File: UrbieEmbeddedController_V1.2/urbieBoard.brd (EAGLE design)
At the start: 100 x 80 mm, 84 parts, among them IC1 IC_FT311D-LQFP-32, J1 DURACLIK-4SMD, Q1 PFET, Q2 2N3904, U2 MAX232TSSOP, Y3 12mHz

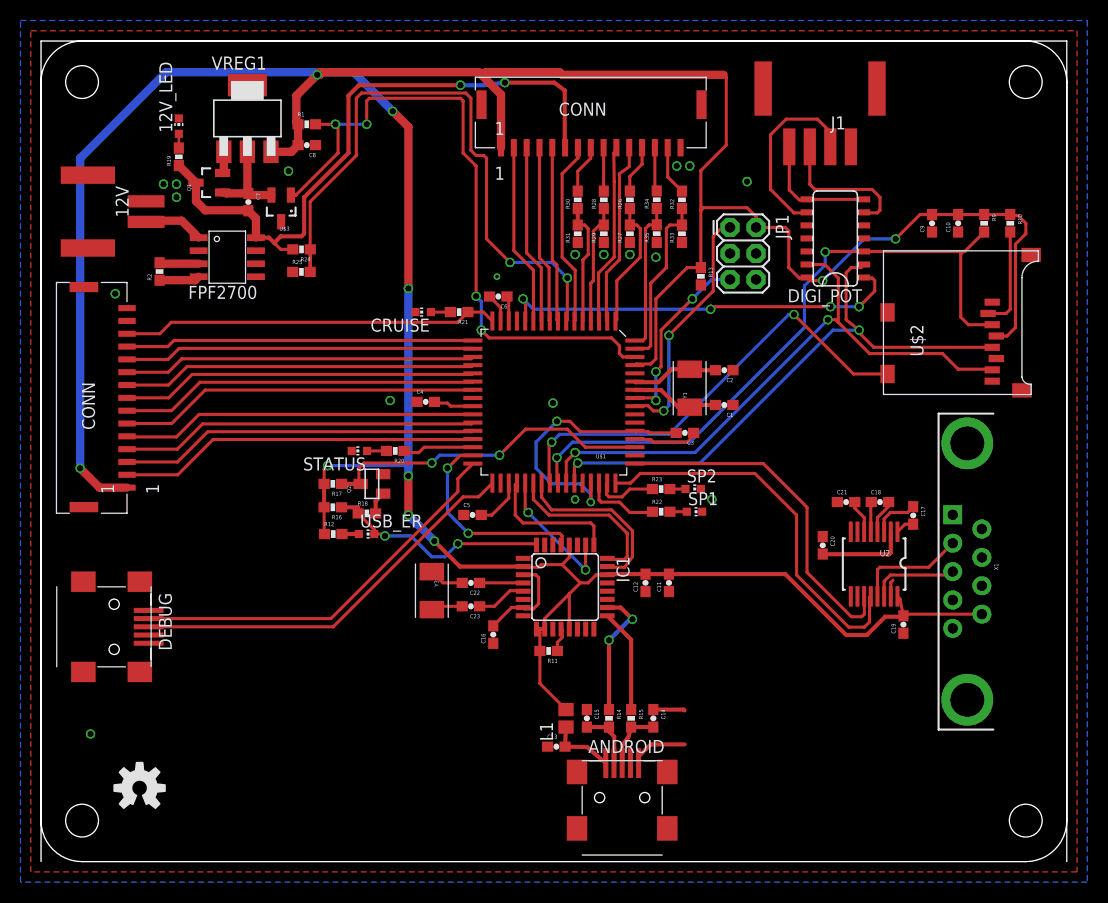
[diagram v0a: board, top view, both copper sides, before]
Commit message: Additions to Version 1.2
Added the 12V to 5V regulator circuit
Fixed SPI SS lines
Added SPI Header
Added TWI Header
Added Silkscreen
TODO: Adjust voltage divider values to get max 2.5V for ADCs
TODO: Pull TWI lines to high
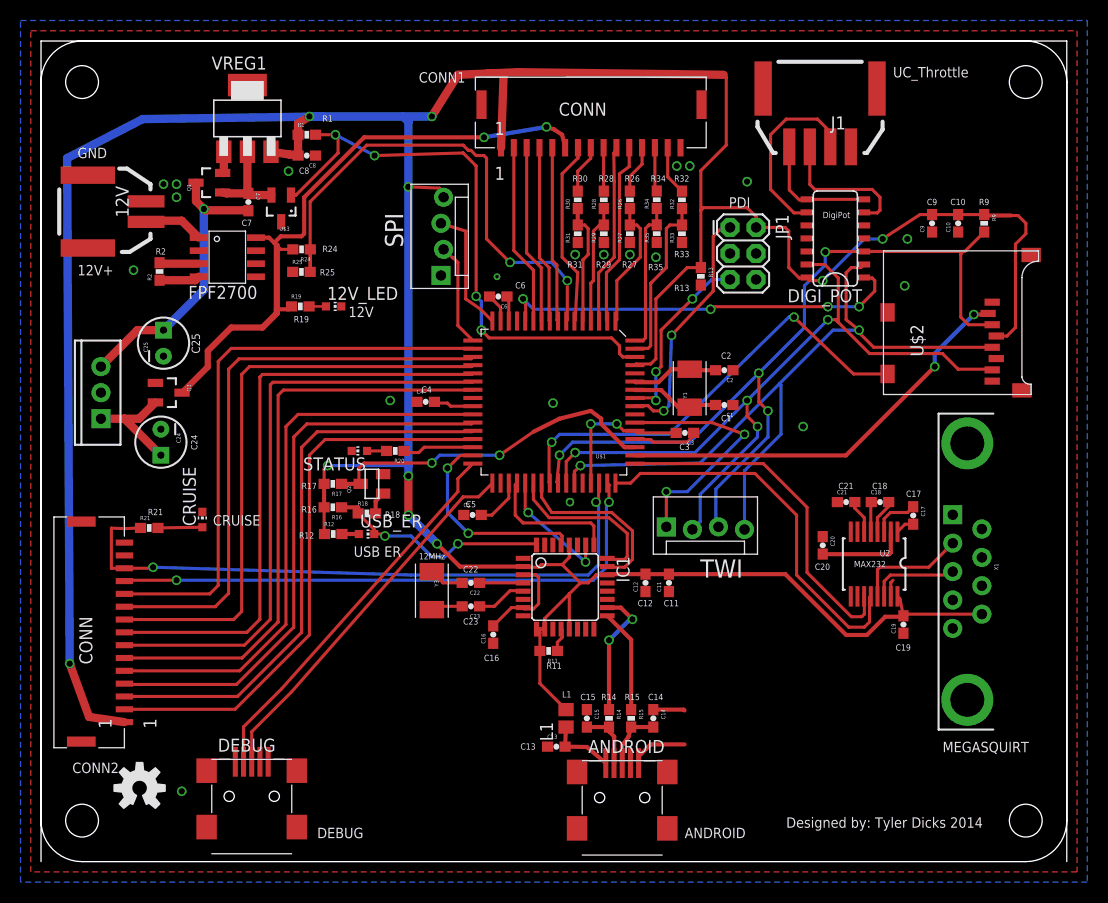
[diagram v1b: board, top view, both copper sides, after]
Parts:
- removed R10: 100K, SparkFun-Passives:0603-RES
- removed R22, R23: 620, SparkFun-Passives:0603-RES
- removed SP1, SP2: (no value), adafruit:CHIP-LED0603
- added C24, C25: (no value), SparkFun-Passives:CPOL-RADIAL-10UF-25V
- added IC2: (no value), SparkFun-PowerIC:TO220-IGO
- added JP3: (no value), SparkFun-Connectors:MOLEX-1X4_LOCK
- added Q3: MOSFET-PCHANNELSMD, SparkFun-DiscreteSemi:SOT23-3
- added SPI: SPI, SparkFun-Connectors:MOLEX-1X4_LOCK
- moved R21 36.8 mm to (10.5, 32.5), turned to 0 degrees
- moved U$6 30.5 mm to (67.6, 7.37)
- moved CRUISE 29.5 mm to (15.7, 33.4), turned to 0 degrees
- moved 12V_LED 23.2 mm to (28.5, 54.1), turned to 270 degrees
- moved U$9 22.9 mm to (8.13, 22.4)
- moved DEBUG 22.7 mm to (20.5, 5.37), turned to 0 degrees
- moved U$5 22.5 mm to (27.7, 7.62)
- moved U$4 21.9 mm to (28.2, 13.0)
- moved R19 18.8 mm to (25.3, 54.1), turned to 0 degrees
- moved R1 1.02 mm to (25.9, 70.9)
- moved C8 1.02 mm to (25.9, 68.8)
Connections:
- removed net CRUISE_ENABLE: U$9.14
- removed net N$17: R10.2, U$2.2
- removed net N$32: R22.2, SP1.A
- removed net N$34: R23.2, SP2.A
- removed net SPARE: U$1.50
- removed net SPARE_LED1: R22.1, U$1.46
- removed net SPARE_LED2: R23.1, U$1.47
- new net 5V_REG: C25.1, C7.2, IC2.OUT, Q1.3
- new net I2C_SCL: JP3.2, U$1.17
- new net I2C_SDA: JP3.3, U$1.16
- new net N$14: C24.1, IC2.IN, Q3.2
- new net SD_CS: U$1.50, U$2.2
- net 3.3V: now also JP3.4; no longer R10.1
- net CRUISE_ON: now also U$1.46; no longer U$1.16
- net DRIVE_ENABLE: now also U$1.47; no longer U$1.17
- net GND: now also C24.2, C25.2, IC2.GND, JP3.1, Q3.1; no longer SP1.C, SP2.C
- net SD_MISO: now also SPI.2
- net SD_MOSI: now also SPI.3
- net SD_SCK: now also SPI.4
- net SPARE2: now also SPI.1
- net V_BATT: now also Q3.3; no longer C7.2, Q1.3
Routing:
- net SD_CS: track 0.00 -> 40.9 mm, vias 0 -> 2
- net 5V_REG: track 0.00 -> 28.3 mm, vias 0 -> 1
- net CRUISE_ON: track 36.9 -> 62.9 mm, vias 0 -> 2
- net SPARE2: track 0.00 -> 24.2 mm, vias 0 -> 2
- net CAP_ON: track 34.7 -> 58.3 mm
- net GEN_STOP: track 34.5 -> 57.8 mm
- net MC_ON: track 34.9 -> 58.0 mm
- net MC_ENABLE: track 35.1 -> 57.7 mm
- net GEN_START: track 34.3 -> 56.9 mm
- net DRIVE_DISABLE: track 34.2 -> 56.7 mm
- net DRIVE_ENABLE: track 34.0 -> 56.1 mm, vias 0 -> 2
- net EFI_IN: track 34.7 -> 55.6 mm
- net STARTING_IN: track 34.8 -> 55.4 mm
- net MC_ON_IN: track 35.0 -> 55.3 mm
- net MC_ENABLE_IN: track 35.2 -> 55.2 mm
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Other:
- board text added: "12MHz"
- board text added: "12V"
- board text added: "12V+"
- board text added: "ANDROID"
- board text added: "C1"
- board text added: "C10"
- board text added: "C11"
- board text added: "C12"
- board text added: "C13"
- board text added: "C14"
- board text added: "C15"
- board text added: "C16"
- board text added: "C17"
- board text added: "C18"
- board text added: "C19"
- board text added: "C2"
- board text added: "C20"
- board text added: "C21"
- board text added: "C22"
- board text added: "C23"
- board text added: "C24"
- board text added: "C25"
- board text added: "C3"
- board text added: "C4"
- board text added: "C5"
- board text added: "C6"
- board text added: "C7"
- board text added: "C8"
- board text added: "C9"
- board text added: "CONN1"
- board text added: "CONN2"
- board text added: "CRUISE"
- board text added: "DEBUG"
- board text added: "Designed by: Tyler Dicks 2014"
- board text added: "DigiPot"
- board text added: "GND"
- board text added: "L1"
- board text added: "MAX232"
- board text added: "MEGASQUIRT"
- board text added: "PDI"
- board text added: "R1"
- board text added: "R11"
- board text added: "R12"
- board text added: "R13"
- board text added: "R14"
- board text added: "R15"
- board text added: "R16"
- board text added: "R17"
- board text added: "R18"
- board text added: "R19"
- board text added: "R2"
- board text added: "R21"
- board text added: "R24"
- board text added: "R25"
- board text added: "R26"
- board text added: "R27"
- board text added: "R28"
- board text added: "R29"
- board text added: "R30"
- board text added: "R31"
- board text added: "R32"
- board text added: "R33"
- board text added: "R34"
- board text added: "R35"
- board text added: "R9"
- board text added: "SPI"
- board text added: "TWI"
- board text added: "UC_Throttle"
- board text added: "USB ER"

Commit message: Fixed ADC values and pin routing
Fixed the voltage divider values to output 2.5V max signal voltage for
ADC
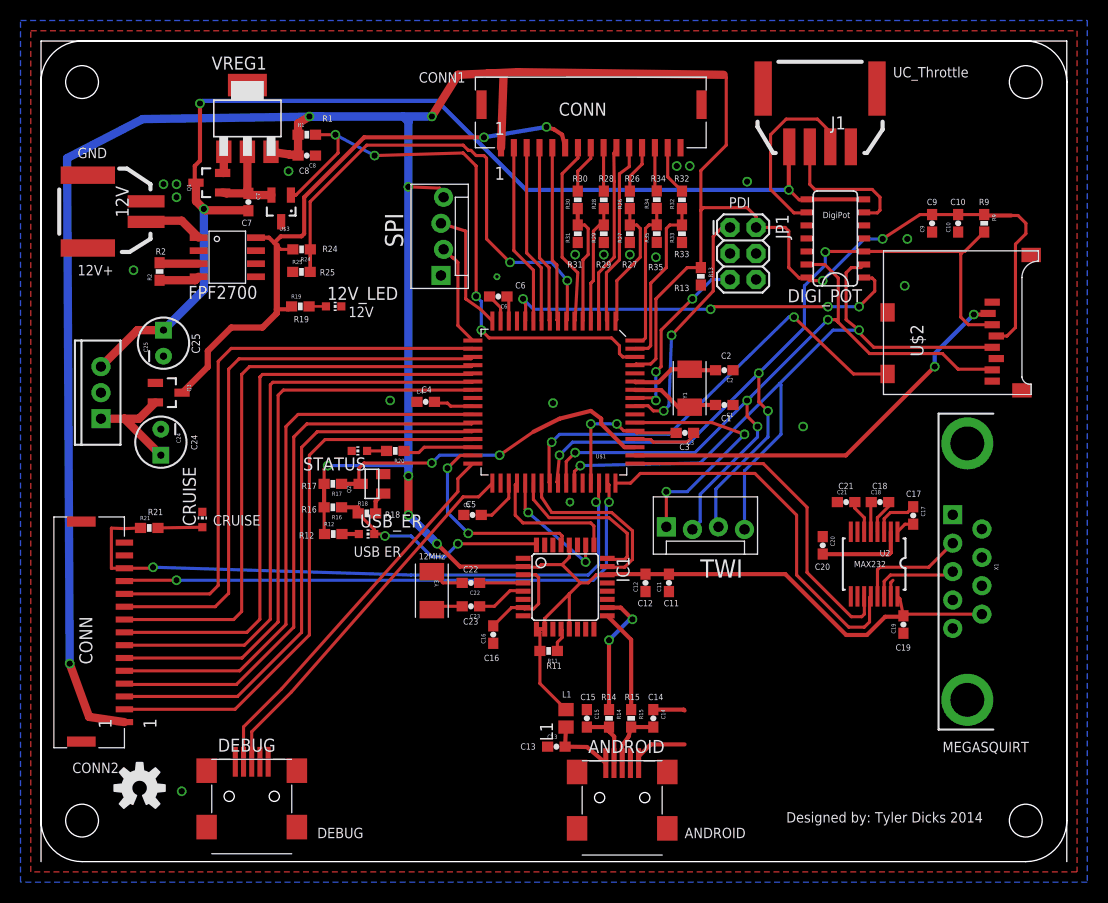
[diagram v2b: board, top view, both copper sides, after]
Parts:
- R25: value 10K -> 7.5K
- R27, R29, R31: value 72K -> 51K
- R33, R35: value 2.2K -> 1.0K
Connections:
- removed net 5V_IN: DIGI_POT.7, DIGI_POT.8, J1.4
- net 5V_REG: now also DIGI_POT.7, DIGI_POT.8, J1.4
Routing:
- net 5V_REG: track 28.3 -> 109.4 mm, vias 1 -> 3
- net 5V_IN: track 11.9 -> 0.00 mm
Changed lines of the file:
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@@
 <text x="36.83" y="75.946" size="1.016" layer="21">CONN1</text>
 <text x="3.048" y="8.636" size="1.016" layer="21">CONN2</text>
-<text x="72.644" y="3.302" size="1.016" layer="21">Designed by: Tyler Dicks 2014</text>
+<text x="72.644" y="3.81" size="1.016" layer="21">Designed by: Tyler Dicks 2014</text>
 <text x="3.556" y="57.15" size="1.016" layer="21">12V+</text>
 <text x="3.556" y="68.58" size="1.016" layer="21">GND</text>
@@
 <element name="R21" library="SparkFun-Passives" package="0603-RES" value="620" x="10.548" y="32.533"/>
 <element name="R24" library="SparkFun-Passives" package="0603-RES" value="33K" x="25.4" y="59.69" rot="R180"/>
-<element name="R25" library="SparkFun-Passives" package="0603-RES" value="10K" x="25.387" y="57.493"/>
+<element name="R25" library="SparkFun-Passives" package="0603-RES" value="7.5K" x="25.387" y="57.493"/>
 <element name="R26" library="SparkFun-Passives" package="0603-RES" value="1M" x="57.404" y="64.516" rot="R90"/>
-<element name="R27" library="SparkFun-Passives" package="0603-RES" value="72K" x="57.404" y="61.214" rot="R90"/>
+<element name="R27" library="SparkFun-Passives" package="0603-RES" value="51K" x="57.404" y="61.214" rot="R90"/>
 <element name="R28" library="SparkFun-Passives" package="0603-RES" value="1M" x="54.864" y="64.516" rot="R90"/>
-<element name="R29" library="SparkFun-Passives" package="0603-RES" value="72K" x="54.864" y="61.214" rot="R90"/>
+<element name="R29" library="SparkFun-Passives" package="0603-RES" value="51K" x="54.864" y="61.214" rot="R90"/>
 <element name="12V" library="Senior Design" package="DURACLIK-2" value="" x="6.779" y="63.371" rot="R270"/>
 <element name="R30" library="SparkFun-Passives" package="0603-RES" value="1M" x="52.324" y="64.516" rot="R90"/>
-<element name="R31" library="SparkFun-Passives" package="0603-RES" value="72K" x="52.324" y="61.214" rot="R90"/>
+<element name="R31" library="SparkFun-Passives" package="0603-RES" value="51K" x="52.324" y="61.214" rot="R90"/>
 <element name="DIGI_POT" library="SparkFun-AnalogIC" package="SO014" value="MCP42XXX" x="77.437" y="60.12" rot="R90"/>
 <element name="R32" library="SparkFun-Passives" package="0603-RES" value="1.1K" x="62.484" y="64.516" rot="R90"/>
-<element name="R33" library="SparkFun-Passives" package="0603-RES" value="2.2K" x="62.484" y="61.214" rot="R90"/>
+<element name="R33" library="SparkFun-Passives" package="0603-RES" value="1.0K" x="62.484" y="61.214" rot="R90"/>
 <element name="R34" library="SparkFun-Passives" package="0603-RES" value="1.1K" x="60.026" y="64.534" rot="R90"/>
-<element name="R35" library="SparkFun-Passives" package="0603-RES" value="2.2K" x="60.026" y="61.224" rot="R90"/>
+<element name="R35" library="SparkFun-Passives" package="0603-RES" value="1.0K" x="60.026" y="61.224" rot="R90"/>
 <element name="LOGO1" library="SparkFun-Aesthetics" package="OSHW-LOGO-M" value="OSHW-LOGOM" x="9.608" y="7.174"/>
 <element name="PCB1" library="dp_devices" package="DP10080_V1" value="PCB_DP_RECTANGLE-80X100" x="50" y="40">
@@
 <wire x1="52.324" y1="67.31" x2="52.324" y2="65.366" width="0.3048" layer="1"/>
 </signal>
-<signal name="5V_IN">
-<contactref element="DIGI_POT" pad="7"/>
-<contactref element="DIGI_POT" pad="8"/>
-<contactref element="J1" pad="4"/>
-<wire x1="80.237" y1="64.565" x2="74.637" y2="64.565" width="0.3048" layer="1"/>
-<wire x1="72.946" y1="69.687" x2="72.946" y2="65.484" width="0.3048" layer="1"/>
-<wire x1="72.946" y1="65.484" x2="73.914" y2="64.516" width="0.3048" layer="1"/>
-<wire x1="73.914" y1="64.516" x2="74.588" y2="64.516" width="0.3048" layer="1"/>
-<wire x1="74.588" y1="64.516" x2="74.637" y2="64.565" width="0.3048" layer="1"/>
-</signal>
 <signal name="THROTTLE_OUT">
 <contactref element="DIGI_POT" pad="6"/>
@@
 <wire x1="5.842" y1="48.26" x2="9.398" y2="51.816" width="0.8128" layer="1"/>
 <wire x1="9.398" y1="51.816" x2="11.938" y2="51.816" width="0.8128" layer="1"/>
+<contactref element="J1" pad="4"/>
+<contactref element="DIGI_POT" pad="7"/>
+<contactref element="DIGI_POT" pad="8"/>
+<wire x1="72.946" y1="65.484" x2="73.914" y2="64.516" width="0.3048" layer="1"/>
+<wire x1="73.914" y1="64.516" x2="74.588" y2="64.516" width="0.3048" layer="1"/>
+<wire x1="74.588" y1="64.516" x2="74.637" y2="64.565" width="0.3048" layer="1"/>
+<wire x1="72.946" y1="65.484" x2="72.898" y2="65.484" width="0.4064" layer="1"/>
+<wire x1="72.898" y1="65.484" x2="72.898" y2="69.088" width="0.4064" layer="1"/>
+<wire x1="72.898" y1="69.088" x2="72.946" y2="69.088" width="0.4064" layer="1"/>
+<wire x1="72.946" y1="69.088" x2="72.946" y2="69.687" width="0.4064" layer="1"/>
+<wire x1="80.237" y1="64.565" x2="74.637" y2="64.565" width="0.4064" layer="1"/>
+<via x="72.898" y="65.484" extent="1-16" drill="0.6"/>
+<wire x1="72.898" y1="65.484" x2="47.292" y2="65.484" width="0.4064" layer="16"/>
+<wire x1="47.292" y1="65.484" x2="38.608" y2="74.168" width="0.4064" layer="16"/>
+<wire x1="38.608" y1="74.168" x2="15.748" y2="74.168" width="0.4064" layer="16"/>
+<wire x1="15.748" y1="74.168" x2="15.494" y2="73.914" width="0.4064" layer="16"/>
+<via x="15.494" y="73.914" extent="1-16" drill="0.6"/>
+<wire x1="15.494" y1="73.914" x2="15.494" y2="68.326" width="0.4064" layer="1"/>
+<wire x1="15.494" y1="68.326" x2="14.986" y2="67.818" width="0.4064" layer="1"/>
+<wire x1="14.986" y1="67.818" x2="14.986" y2="66.308" width="0.4064" layer="1"/>
+<wire x1="14.986" y1="66.308" x2="15.106" y2="66.188" width="0.4064" layer="1"/>
 </signal>
 </signals>

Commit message: small aesthetic fixes
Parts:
- moved U$6 2.81 mm to (64.8, 7.62)
- moved U$4 2.40 mm to (30.2, 11.7)
- moved U$5 2.27 mm to (29.7, 6.60)
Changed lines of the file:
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@@
 <element name="U$8" library="FPF2700" package="FPF2700" value="FPF2700" x="18.161" y="58.928" rot="R90"/>
 <element name="R2" library="SparkFun-Passives" package="0603-RES" value="110K" x="11.557" y="57.531" rot="R90"/>
-<element name="U$4" library="Senior Design" package="SHELL" value="" x="28.194" y="12.954"/>
-<element name="U$5" library="Senior Design" package="SEM" value="" x="27.686" y="7.62"/>
-<element name="U$6" library="Senior Design" package="CU-PILLAR" value="" x="67.564" y="7.366"/>
+<element name="U$4" library="Senior Design" package="SHELL" value="" x="30.226" y="11.684"/>
+<element name="U$5" library="Senior Design" package="SEM" value="" x="29.718" y="6.604"/>
+<element name="U$6" library="Senior Design" package="CU-PILLAR" value="" x="64.77" y="7.62"/>
 <element name="Y3" library="SparkFun-FreqCtrl" package="CRYSTAL-TXC-7A" value="12mHz" x="38.1" y="26.416" rot="R270"/>
 <element name="C22" library="SparkFun-Capacitors" package="0603-CAP" value="18pF" x="41.91" y="27.178" rot="R180"/>

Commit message: Gerbers and connector changes
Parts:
- removed ANDROID: (no value), adafruit:USB-MINIB
- removed DIGI_POT: MCP42XXX, SparkFun-AnalogIC:SO014
- removed J1: DURACLIK-4SMD, Senior Design:DURACLIK-4
- removed Q1: PFET, SparkFun-DiscreteSemi:SOT23-3
- removed Q3: MOSFET-PCHANNELSMD, SparkFun-DiscreteSemi:SOT23-3
- removed U$7, U$9: MOLEX15_PIN, Molex15_pin:MOLEX15PIN
- added JP2: (no value), jumper:JP1
- added JP4: USB-A-S, SparkFun-Connectors:USB-A-S
- added U$10, U$11: 15PIN, 15pinconn:15PIN
- C24, C25: value (none) -> 4.7uF
- Q2: value 2N3904 -> MMBT3904; device SparkFun-DiscreteSemi:SOT23 -> transistor-npn:SOT23-BEC
- moved C13 6.65 mm to (45.7, 16.0)
- moved C3 6.11 mm to (59.3, 36.8)
- moved C14 4.57 mm to (59.7, 18.5)
- moved C15 4.57 mm to (53.2, 18.5)
- moved R14 4.57 mm to (55.4, 18.5)
- moved R15 4.57 mm to (57.5, 18.5)
- moved L1 3.78 mm to (48.6, 16.8)
- moved SPI 2.05 mm to (63.0, 32.8)
- moved R21 1.02 mm to (11.6, 32.5)
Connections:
- removed net N$14: C24.1, IC2.IN, Q3.2
- removed net N$3: Q1.2, VREG1.1
- removed net N$4: C6.2, U$1.15
- removed net N$5: C4.2, U$1.25
- removed net N$6: C5.2, U$1.35
- removed net N$7: C3.2, U$1.45, U$1.53
- removed net REGEN_OUT: DIGI_POT.9, J1.2
- removed net THROTTLE_OUT: DIGI_POT.6, J1.3
- net 3.3V: now also C3.2, C4.2, C5.2, C6.2, U$1.15, U$1.25, U$1.35, U$1.45, U$1.53, U$10.PIN1, U$11.PIN1; no longer DIGI_POT.14, U$7.1, U$9.1
- net 5V_REG: now also VREG1.1; no longer DIGI_POT.7, DIGI_POT.8, J1.4, Q1.3
- net ANDROID_D+: now also JP4.D+; no longer ANDROID.D+
- net ANDROID_D-: now also JP4.D-; no longer ANDROID.D-
- net ANDR_ENABLE: now also Q2.C; no longer Q2.3
- net CAP_ON: now also U$11.PIN8; no longer U$9.8
- net CAP_V_IN: now also U$10.PIN12; no longer U$7.12
- net CRUISE_ON: now also U$11.PIN13; no longer U$9.13
- net DIGI_POT_SEL: no longer DIGI_POT.1
- net DRIVE_CUR: now also U$10.PIN11; no longer U$7.11
- net DRIVE_DISABLE: now also U$11.PIN11; no longer U$9.11
- net DRIVE_ENABLE: now also U$11.PIN12; no longer U$9.12
- net DRIVE_ENABLE_IN: now also U$10.PIN2; no longer U$7.2
- net DRIVE_V_IN: now also U$10.PIN9; no longer U$7.9
- net EFI_IN: now also U$11.PIN5; no longer U$9.5
- net GEN_CUR: now also U$10.PIN10; no longer U$7.10
- net GEN_START: now also U$11.PIN10; no longer U$9.10
- net GEN_STOP: now also U$11.PIN9; no longer U$9.9
- net GEN_TEMP: now also U$10.PIN5; no longer U$7.5
- net GEN_V_IN: now also U$10.PIN8; no longer U$7.8
- net GND: now also JP4.GND, Q2.E, U$10.PIN15, U$11.PIN15; no longer ANDROID.GND, DIGI_POT.10, DIGI_POT.11, DIGI_POT.12, DIGI_POT.4, DIGI_POT.5, J1.1, Q1.1, Q2.2, Q3.1, U$7.15, U$9.15
- net MC_ENABLE: now also U$11.PIN6; no longer U$9.6
- net MC_ENABLE_IN: now also U$11.PIN2; no longer U$9.2
- net MC_ON: now also U$11.PIN7; no longer U$9.7
- net MC_ON_IN: now also U$11.PIN3; no longer U$9.3
- net MOTOR_TEMP: now also U$10.PIN4; no longer U$7.4
- net N$23: now also Q2.B; no longer Q2.1
- net N$24: now also JP4.VBUS; no longer ANDROID.VBUS
- net PITOT: now also U$10.PIN7; no longer U$7.7
- net REGEN_POS: now also U$10.PIN13; no longer U$7.13
- net SD_MISO: no longer DIGI_POT.13
- net SD_MOSI: no longer DIGI_POT.3
- net SD_SCK: no longer DIGI_POT.2
- net SPEED: now also U$10.PIN3; no longer U$7.3
- net STARTING_IN: now also U$11.PIN4; no longer U$9.4
- net THROTTLE_POS: now also U$10.PIN14; no longer U$7.14
- net V_BATT: now also C24.1, IC2.IN, JP2.1, U$10.PIN6; no longer Q3.3, U$7.6
- net V_BATT_IN: now also JP2.2
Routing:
- net 5V_REG: track 109.4 -> 32.6 mm, vias 3 -> 1
- net 3.3V: track 373.1 -> 439.8 mm, vias 10 -> 11
- net DIGI_POT_SEL: track 39.9 -> 0.00 mm, vias 4 -> 0
- net REGEN_OUT: track 18.2 -> 0.00 mm
- net V_BATT: track 61.6 -> 77.9 mm
- net N$7: track 14.5 -> 0.00 mm, vias 2 -> 0
- net THROTTLE_OUT: track 14.0 -> 0.00 mm
- net N$14: track 11.0 -> 0.00 mm
- net SD_SCK: track 72.3 -> 62.5 mm
- net V_BATT_IN: track 6.09 -> 15.9 mm
- net SD_MISO: track 75.0 -> 65.5 mm
- net GND: track 32.2 -> 24.9 mm, vias 20 -> 25
- net SD_MOSI: track 83.8 -> 76.8 mm
- net N$6: track 4.84 -> 0.00 mm
- net N$19: track 10.1 -> 5.54 mm
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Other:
- board text removed: "UC_Throttle"
